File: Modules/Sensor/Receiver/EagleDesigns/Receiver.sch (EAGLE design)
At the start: 11 parts, among them U2 ATMEGA328P_TQFP

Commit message: fixed eagle files for new modules
SIN/SOUT was not correctly connected in them.
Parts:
- C3: device adafruit:C-USC0402 -> adafruit:C-USC0603
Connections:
- removed net 1X3SIN-SOUT: JP1.1, JP1.4, R1.2
- net 1X3SIN: now also JP1.4, R1.2
- net 1X3SOUT: now also JP1.1
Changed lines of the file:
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@@
 <part name="GND3" library="SparkFun-Aesthetics" deviceset="GND" device=""/>
 <part name="R4" library="adafruit" deviceset="R-US_" device="R0603" value="4.7K"/>
-<part name="C3" library="adafruit" deviceset="C-US" device="C0402" value="0.22uF"/>
 <part name="U$1" library="tsop" deviceset="TSOP38238" device=""/>
 <part name="GND4" library="SparkFun-Aesthetics" deviceset="GND" device=""/>
 <part name="SUPPLY3" library="SparkFun-Aesthetics" deviceset="VCC" device=""/>
+<part name="C3" library="adafruit" deviceset="C-US" device="C0603" value="0.22uF"/>
 </parts>
 <sheets>
@@
 <instance part="GND3" gate="1" x="322.58" y="-17.78"/>
 <instance part="R4" gate="G$1" x="309.88" y="27.94" rot="R180"/>
-<instance part="C3" gate="G$1" x="322.58" y="5.08"/>
 <instance part="U$1" gate="G$1" x="243.84" y="27.94"/>
 <instance part="GND4" gate="1" x="254" y="-17.78"/>
 <instance part="SUPPLY3" gate="G$1" x="254" y="73.66"/>
+<instance part="C3" gate="G$1" x="322.58" y="5.08"/>
 </instances>
 <busses>
@@
 <wire x1="254" y1="22.86" x2="254" y2="-15.24" width="0.1524" layer="91"/>
 <pinref part="GND4" gate="1" pin="GND"/>
-</segment>
-</net>
-<net name="1X3SIN-SOUT" class="0">
-<segment>
-<pinref part="JP1" gate="G$1" pin="4"/>
-<wire x1="10.16" y1="33.02" x2="35.56" y2="33.02" width="0.1524" layer="91"/>
-<label x="17.78" y="33.02" size="1.778" layer="95"/>
-<junction x="35.56" y="33.02"/>
-</segment>
-<segment>
-<pinref part="JP1" gate="G$1" pin="1"/>
-<wire x1="10.16" y1="25.4" x2="35.56" y2="25.4" width="0.1524" layer="91"/>
-<label x="17.78" y="25.4" size="1.778" layer="95"/>
-<junction x="35.56" y="25.4"/>
-</segment>
-<segment>
-<wire x1="58.42" y1="30.48" x2="78.74" y2="30.48" width="0.1524" layer="91"/>
-<junction x="78.74" y="30.48"/>
-<wire x1="58.42" y1="20.32" x2="58.42" y2="30.48" width="0.1524" layer="91"/>
-<label x="60.96" y="30.48" size="1.778" layer="95"/>
-<pinref part="R1" gate="G$1" pin="2"/>
 </segment>
 </net>
@@
 <label x="210.82" y="55.88" size="1.778" layer="95"/>
 </segment>
+<segment>
+<pinref part="JP1" gate="G$1" pin="4"/>
+<wire x1="10.16" y1="33.02" x2="35.56" y2="33.02" width="0.1524" layer="91"/>
+<label x="17.78" y="33.02" size="1.778" layer="95"/>
+<junction x="35.56" y="33.02"/>
+</segment>
+<segment>
+<wire x1="58.42" y1="30.48" x2="78.74" y2="30.48" width="0.1524" layer="91"/>
+<junction x="78.74" y="30.48"/>
+<wire x1="58.42" y1="20.32" x2="58.42" y2="30.48" width="0.1524" layer="91"/>
+<label x="60.96" y="30.48" size="1.778" layer="95"/>
+<pinref part="R1" gate="G$1" pin="2"/>
+</segment>
 </net>
 <net name="N$1" class="0">
@@
 <pinref part="C3" gate="G$1" pin="1"/>
 </segment>
-</net>
+<segment>
+<pinref part="JP1" gate="G$1" pin="1"/>
+<wire x1="10.16" y1="25.4" x2="35.56" y2="25.4" width="0.1524" layer="91"/>
+<label x="17.78" y="25.4" size="1.778" layer="95"/>
+<junction x="35.56" y="25.4"/>
+</segment>
+</net>

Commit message: Receiver: added final PCB #29
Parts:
- U$1: value TSOP38238 -> IR-RECEIVER; device tsop:TSOP38238 -> MakerWear:IR-RECEIVER
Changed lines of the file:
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@@
 <part name="GND3" library="SparkFun-Aesthetics" deviceset="GND" device=""/>
 <part name="R4" library="adafruit" deviceset="R-US_" device="R0603" value="4.7K"/>
-<part name="U$1" library="tsop" deviceset="TSOP38238" device=""/>
 <part name="GND4" library="SparkFun-Aesthetics" deviceset="GND" device=""/>
 <part name="SUPPLY3" library="SparkFun-Aesthetics" deviceset="VCC" device=""/>
 <part name="C3" library="adafruit" deviceset="C-US" device="C0603" value="0.22uF"/>
+<part name="U$1" library="MakerWear" deviceset="IR-RECEIVER" device=""/>
 </parts>
 <sheets>
@@
 <instance part="GND3" gate="1" x="322.58" y="-17.78"/>
 <instance part="R4" gate="G$1" x="309.88" y="27.94" rot="R180"/>
-<instance part="U$1" gate="G$1" x="243.84" y="27.94"/>
 <instance part="GND4" gate="1" x="254" y="-17.78"/>
 <instance part="SUPPLY3" gate="G$1" x="254" y="73.66"/>
 <instance part="C3" gate="G$1" x="322.58" y="5.08"/>
+<instance part="U$1" gate="G$1" x="243.84" y="27.94"/>
 </instances>
 <busses>
@@
 </segment>
 <segment>
-<pinref part="U$1" gate="G$1" pin="V+"/>
 <wire x1="251.46" y1="33.02" x2="254" y2="33.02" width="0.1524" layer="91"/>
 <wire x1="254" y1="33.02" x2="254" y2="73.66" width="0.1524" layer="91"/>
 <pinref part="SUPPLY3" gate="G$1" pin="VCC"/>
+<pinref part="U$1" gate="G$1" pin="V+"/>
 </segment>
 </net>
@@
 </segment>
 <segment>
-<pinref part="U$1" gate="G$1" pin="GND"/>
 <wire x1="251.46" y1="22.86" x2="254" y2="22.86" width="0.1524" layer="91"/>
 <wire x1="254" y1="22.86" x2="254" y2="-15.24" width="0.1524" layer="91"/>
 <pinref part="GND4" gate="1" pin="GND"/>
+<pinref part="U$1" gate="G$1" pin="GND"/>
 </segment>
 </net>
@@
 </segment>
 <segment>
-<pinref part="U$1" gate="G$1" pin="OUT"/>
 <wire x1="251.46" y1="27.94" x2="266.7" y2="27.94" width="0.1524" layer="91"/>
 <junction x="266.7" y="27.94"/>
 <label x="259.08" y="27.94" size="1.778" layer="95"/>
-</segment>
-</net>
+<pinref part="U$1" gate="G$1" pin="OUT"/>
+</segment>
+</net>

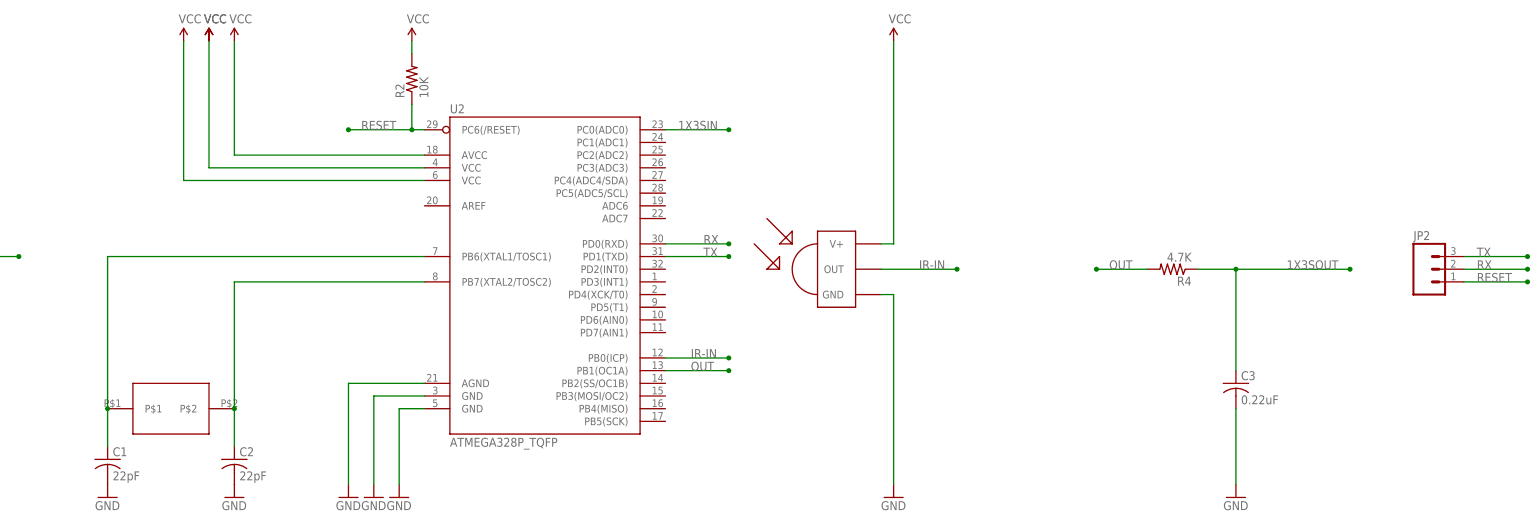
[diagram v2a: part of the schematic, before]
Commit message: Receiver: removed crystal, modified to work with new bootloader #29
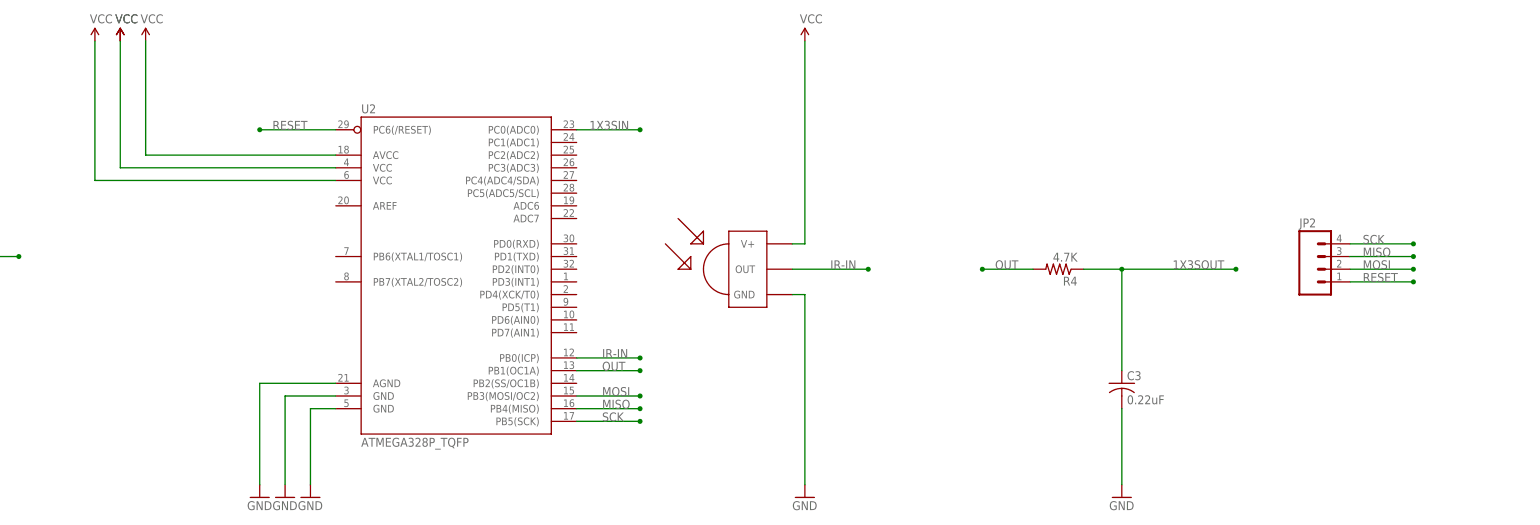
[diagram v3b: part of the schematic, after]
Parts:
- removed C1, C2: 22pF, adafruit:C-USC0603
- removed R2: 10K, resistor:R-US_R0603
- removed U$2: NX503, MakerWear:NX503
- JP2: device SparkFun-Connectors:M03PTH -> SparkFun-Connectors:M04PTH
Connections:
- removed net N$1: C1.1, U$2.P$1, U2.PB6(XTAL1/TOSC1)
- removed net N$3: C2.1, U$2.P$2, U2.PB7(XTAL2/TOSC2)
- removed net RX: JP2.2, U2.PD0(RXD)
- removed net TX: JP2.3, U2.PD1(TXD)
- new net MISO: JP2.3, U2.PB4(MISO)
- new net MOSI: JP2.2, U2.PB3(MOSI/OC2)
- new net SCK: JP2.4, U2.PB5(SCK)
- net GND: no longer C1.2, C2.2
- net RESET: no longer R2.1
- net VCC: no longer R2.2
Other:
- moved on the sheet: C3, R4, U2
